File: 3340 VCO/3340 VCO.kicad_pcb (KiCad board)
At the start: 2 copper layers, 99 parts, among them J1 AudioJack2_SwitchT, J2 AudioJack2_SwitchT, J3 AudioJack2_SwitchT, J4 AudioJack2_SwitchT, J5 AudioJack2_SwitchT, J6 Conn_02x05_Odd_Even, J7 AudioJack2_SwitchT, J8 AudioJack2_SwitchT, J9 AudioJack2_SwitchT, SW1 SW_SPDT, U1 TL072, U2 TL072, U3 TL072, U4 AS3340

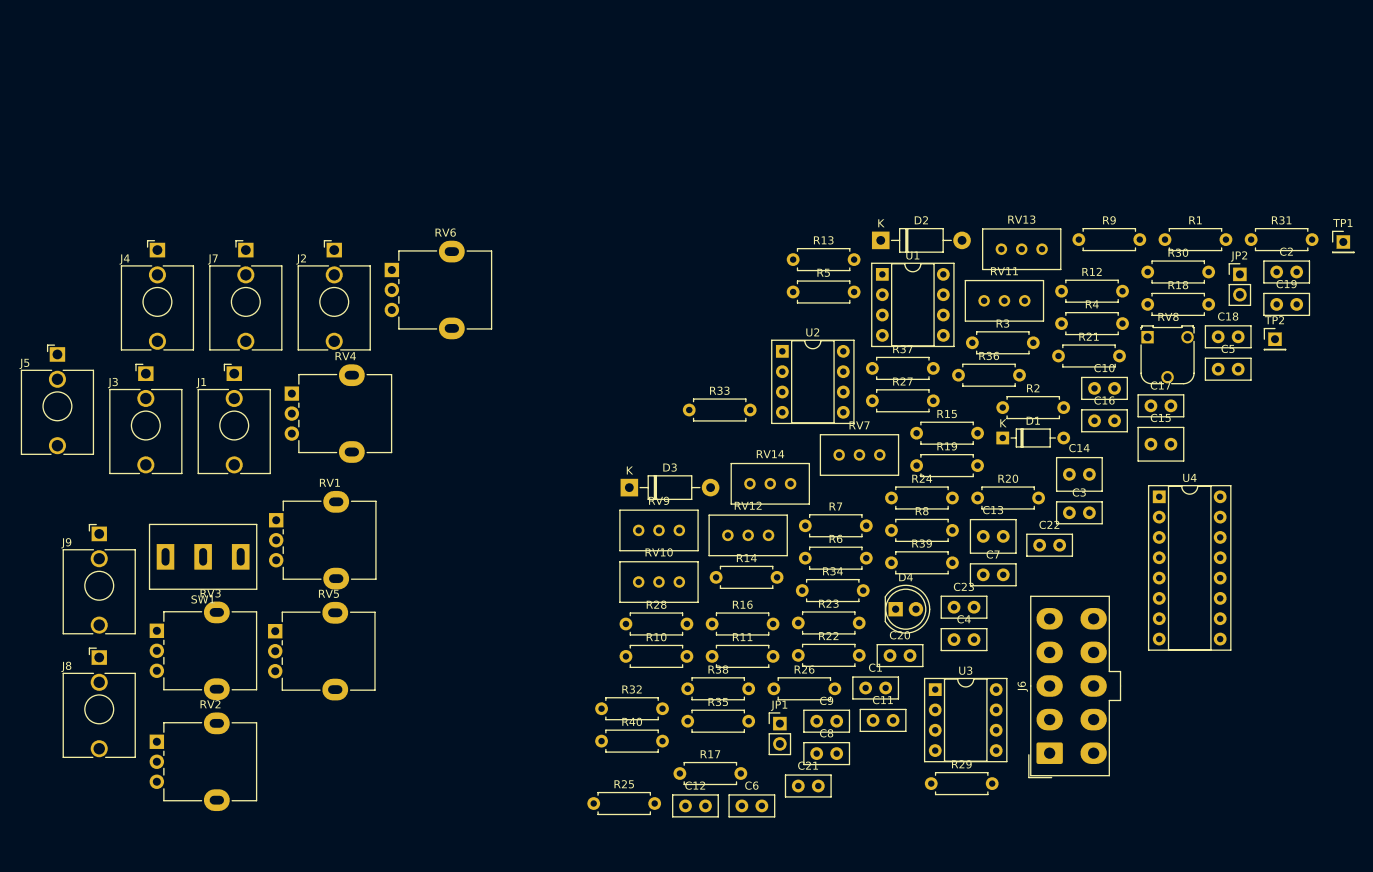
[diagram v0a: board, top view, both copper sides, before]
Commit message: Create separate front end VCO board
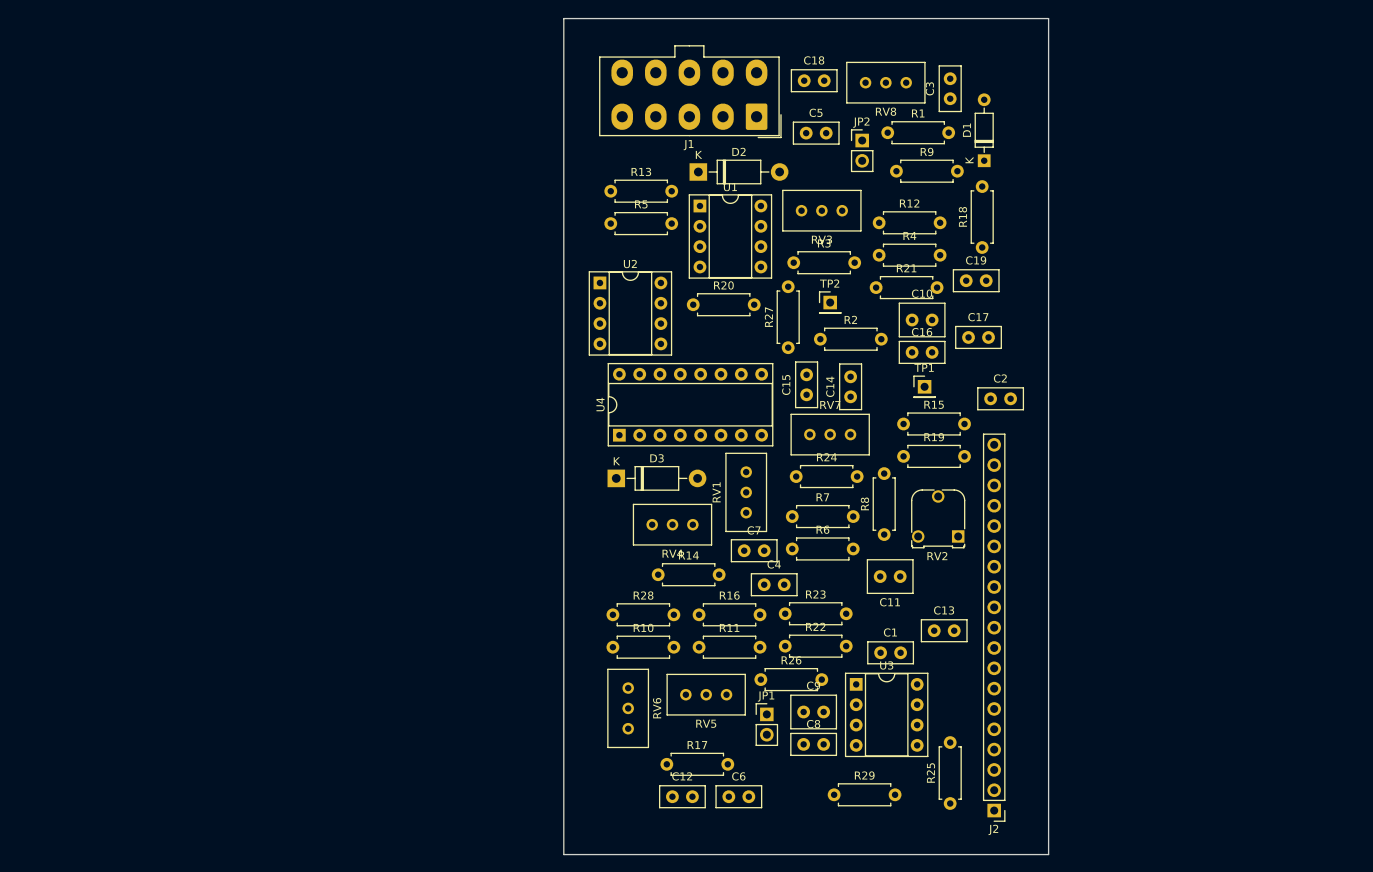
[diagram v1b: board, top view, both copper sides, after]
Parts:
- removed C20, C21, C22: 10p, 0_Capacitor_THT:C_Disc_D5.5mm_W2.5mm_P2.50mm
- removed C23: 47n, 0_Capacitor_THT:C_Disc_D5.5mm_W2.5mm_P2.50mm
- removed D4: LED, LED_THT:LED_D5.0mm
- removed J3, J4, J5, J7, J8, J9: AudioJack2_SwitchT, Connector_Audio:Jack_3.5mm_QingPu_WQP-PJ398SM_Vertical_CircularHoles
- removed J6: Conn_02x05_Odd_Even, Connector_Molex:Molex_Mini-Fit_Jr_5566-10A_2x05_P4.20mm_Vertical
- removed R30, R37: 47k, Resistor_THT:R_Axial_DIN0207_L6.3mm_D2.5mm_P7.62mm_Horizontal
- removed R31: 56k, Resistor_THT:R_Axial_DIN0207_L6.3mm_D2.5mm_P7.62mm_Horizontal
- removed R32: 75k, Resistor_THT:R_Axial_DIN0207_L6.3mm_D2.5mm_P7.62mm_Horizontal
- removed R33, R34, R35: 1k, Resistor_THT:R_Axial_DIN0207_L6.3mm_D2.5mm_P7.62mm_Horizontal
- removed R36: 68k, Resistor_THT:R_Axial_DIN0207_L6.3mm_D2.5mm_P7.62mm_Horizontal
- removed R38: 15k, Resistor_THT:R_Axial_DIN0207_L6.3mm_D2.5mm_P7.62mm_Horizontal
- removed R39, R40: 33k, Resistor_THT:R_Axial_DIN0207_L6.3mm_D2.5mm_P7.62mm_Horizontal
- removed RV10, RV12, RV13, RV14, RV9: 10k, Potentiometer_THT:Potentiometer_Bourns_3296W_Vertical
- removed RV11: 1k, Potentiometer_THT:Potentiometer_Bourns_3296W_Vertical
- removed SW1: SW_SPDT, 0_Switch_THT:MTS-102_MTS-103_MTS-112_MTS-113_MTS-123
- C1: value 0.1u -> 10n
- C10: value 0.1u -> 10u; footprint 0_Capacitor_THT:C_Disc_D5.5mm_W2.5mm_P2.50mm -> 0_Capacitor_THT:C_Disc_D5.5mm_W4.0mm_P2.50mm
- C11: value 0.1u -> 1u; footprint 0_Capacitor_THT:C_Disc_D5.5mm_W2.5mm_P2.50mm -> 0_Capacitor_THT:C_Disc_D5.5mm_W4.0mm_P2.50mm
- C12: value 680p -> 0.1u
- C13, C14: value 10u -> 0.1u; footprint 0_Capacitor_THT:C_Disc_D5.5mm_W4.0mm_P2.50mm -> 0_Capacitor_THT:C_Disc_D5.5mm_W2.5mm_P2.50mm
- C15: value 1u -> 0.1u; footprint 0_Capacitor_THT:C_Disc_D5.5mm_W4.0mm_P2.50mm -> 0_Capacitor_THT:C_Disc_D5.5mm_W2.5mm_P2.50mm
- C16, C17, C18: value 0.1u -> 10p
- C19: value 0.1u -> 47n
- C2: value 1n -> 10p
- C3: value 10p -> 10n
- C4, C5: value 10n -> 0.1u
- C8: value 1n -> 680p
- C9: value 10n -> 10u; footprint 0_Capacitor_THT:C_Disc_D5.5mm_W2.5mm_P2.50mm -> 0_Capacitor_THT:C_Disc_D5.5mm_W4.0mm_P2.50mm
- J1: value AudioJack2_SwitchT -> Conn_02x05_Odd_Even; footprint Connector_Audio:Jack_3.5mm_QingPu_WQP-PJ398SM_Vertical_CircularHoles -> Connector_Molex:Molex_Mini-Fit_Jr_5566-10A_2x05_P4.20mm_Vertical
- J2: value AudioJack2_SwitchT -> Conn_01x19; footprint Connector_Audio:Jack_3.5mm_QingPu_WQP-PJ398SM_Vertical_CircularHoles -> Connector_PinHeader_2.54mm:PinHeader_1x19_P2.54mm_Vertical
- R1: value 100k -> 150k
- R10: value 56k -> 1M
- R11: value 150k -> 15k
- R12: value 470 -> 1.5k
- R13: value 470k -> 510
- R14: value 22k -> 56k
- R15: value 1M -> 56k
- R16, R20: value 1M -> 47k
- R17: value 470 -> 47k
- R18, R19: value 5.6k -> 33k
- R2: value 100k -> 470
- R21: value 15k -> 56k
- R22: value 1.5k -> 75k
- R23: value 510 -> 1k
- R24, R25: value 56k -> 1k
- R26: value 47k -> 68k
- R28: value 33k -> 15k
- R3: value 100k -> 470k
- R4: value 100k -> 56k
- R5: value 100k -> 22k
- R6: value 220k -> 1M
- R7: value 15k -> 470
- R8, R9: value 100k -> 5.6k
- RV1: value 10k -> 100k; footprint 0_Potentiometer_THT:Potentiometer_Alpha_RD901F-40-00D_Single_Vertical_MP -> Potentiometer_THT:Potentiometer_Bourns_3296W_Vertical
- RV2: footprint 0_Potentiometer_THT:Potentiometer_Alpha_RD901F-40-00D_Single_Vertical_MP -> Potentiometer_THT:Potentiometer_Runtron_RM-065_Vertical
- RV3, RV4, RV6: footprint 0_Potentiometer_THT:Potentiometer_Alpha_RD901F-40-00D_Single_Vertical_MP -> Potentiometer_THT:Potentiometer_Bourns_3296W_Vertical
- RV5: value 10k -> 1k; footprint 0_Potentiometer_THT:Potentiometer_Alpha_RD901F-40-00D_Single_Vertical_MP -> Potentiometer_THT:Potentiometer_Bourns_3296W_Vertical
- RV7: value 100k -> 10k
- RV8: footprint Potentiometer_THT:Potentiometer_Runtron_RM-065_Vertical -> Potentiometer_THT:Potentiometer_Bourns_3296W_Vertical
- moved J2 108.2 mm to (168.1, 135.1), turned to 180 degrees
- moved RV2 103.4 mm to (163.6, 100.8), turned to 180 degrees
- moved RV3 96.2 mm to (144.0, 60.1), turned to 180 degrees
- moved J1 72.8 mm to (138.4, 48.3), turned to 180 degrees
- moved U4 67.9 mm to (121.2, 88.2), turned to 90 degrees
- moved RV6 64.5 mm to (122.3, 124.8), turned to -90 degrees
- moved C18 60.8 mm to (144.3, 43.8)
- moved C5 59.4 mm to (144.6, 50.4)
- moved RV1 59.1 mm to (137.1, 92.8), turned to 90 degrees
- moved TP2 55.8 mm to (147.6, 71.6)
- moved TP1 55.4 mm to (159.4, 82.1)
- moved C3 53.9 mm to (162.6, 46.1), turned to 90 degrees
- moved RV5 51.9 mm to (129.5, 120.6), turned to 180 degrees
- moved JP2 50.1 mm to (151.6, 51.3)
- moved RV4 47.9 mm to (125.3, 99.3), turned to 180 degrees
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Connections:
- C1 pad 2: Net-(C1-Pad2) -> GND
- C10 pad 2: +12V -> -12V
- C11 pad 1: -12V -> GND
- C11 pad 2: GND -> Net-(U4-VSSI)
- C12 pad 2: Net-(C12-Pad2) -> Net-(U4-VEE)
- C13 pad 1: +12V -> GND
- C13 pad 2: GND -> +12V
- C14 pad 1: GND -> -12V
- C14 pad 2: -12V -> GND
- C15 pad 2: Net-(C15-Pad2) -> +12V
- C16 pad 1: GND -> Net-(U2A--)
- C17 pad 1: GND -> Net-(U2B--)
- C17 pad 2: +12V -> Net-(C17-Pad2)
- C18 pad 1: -12V -> Net-(U3A--)
- C18 pad 2: GND -> Net-(C18-Pad2)
- C19 pad 1: GND -> Net-(U3B--)
- C19 pad 2: +12V -> /LED
- C2 pad 1: Net-(C2-Pad1) -> /PWM
- C2 pad 2: Net-(C2-Pad2) -> Net-(D1-K)
- C3 pad 2: Net-(C3-Pad2) -> GND
- C4 pad 1: Net-(C4-Pad1) -> GND
- C4 pad 2: GND -> +12V
- C5 pad 1: Net-(C5-Pad1) -> -12V
- C8 pad 2: Net-(C8-Pad2) -> Net-(JP2-B)
- C9 pad 1: GND -> +12V
- C9 pad 2: Net-(C9-Pad2) -> GND
- D1 pad 1: Net-(C3-Pad2) -> Net-(D1-K)
- D1 pad 2: Net-(C3-Pad1) -> /PWM
- JP1 pad 1: Net-(JP1-Pad1) -> /CV
- JP1 pad 2: Net-(JP1-Pad2) -> Net-(JP1-B)
- JP2 pad 2: Net-(C12-Pad2) -> Net-(JP2-B)
- R1 pad 1: +12V -> Net-(R1-Pad1)
- R1 pad 2: Net-(R1-Pad2) -> Net-(JP1-B)
- R10 pad 1: Net-(C3-Pad1) -> Net-(D1-K)
- R10 pad 2: Net-(C3-Pad2) -> Net-(U4-VP)
- R11 pad 1: Net-(R11-Pad1) -> Net-(U4-SCALE1)
- R11 pad 2: Net-(JP1-Pad2) -> Net-(R11-Pad2)
- R12 pad 1: Net-(JP1-Pad2) -> Net-(R12-Pad1)
- R12 pad 2: Net-(C4-Pad1) -> Net-(JP2-B)
- R13 pad 1: Net-(JP1-Pad2) -> Net-(U4-VEE)
- R13 pad 2: Net-(R13-Pad2) -> -12V
- R14 pad 1: Net-(R14-Pad1) -> Net-(U4-VP)
- R14 pad 2: GND -> Net-(U2A--)
- R15 pad 1: Net-(C1-Pad2) -> Net-(R15-Pad1)
- R15 pad 2: Net-(R15-Pad2) -> Net-(U2A--)
- R16 pad 1: Net-(R16-Pad1) -> Net-(U4-VSO)
- R16 pad 2: Net-(R15-Pad2) -> Net-(U2B--)
- R17 pad 1: Net-(R15-Pad2) -> Net-(R17-Pad1)
- R17 pad 2: Net-(C5-Pad1) -> Net-(U2B--)
- R18 pad 1: Net-(C16-Pad2) -> Net-(U1B--)
- R18 pad 2: Net-(R18-Pad2) -> Net-(U3A--)
- R19 pad 1: Net-(C16-Pad2) -> Net-(R19-Pad1)
- R19 pad 2: Net-(R19-Pad2) -> Net-(U3A--)
- R2 pad 1: Net-(R2-Pad1) -> Net-(JP1-B)
- R2 pad 2: -12V -> Net-(C1-Pad1)
- R20 pad 1: Net-(C3-Pad2) -> Net-(U2A--)
- R20 pad 2: Net-(R20-Pad2) -> /PULSE
- R21 pad 1: Net-(R21-Pad1) -> Net-(U2B--)
- R21 pad 2: Net-(R21-Pad2) -> /RAMP
- R22 pad 1: Net-(R22-Pad1) -> Net-(U3A--)
- R22 pad 2: Net-(C12-Pad2) -> /TRI
- R23 pad 2: -12V -> /PULSE
- R24 pad 1: Net-(R20-Pad2) -> Net-(C17-Pad2)
- R24 pad 2: Net-(C20-Pad1) -> /RAMP
- R25 pad 1: Net-(R25-Pad1) -> Net-(C18-Pad2)
- R25 pad 2: Net-(C20-Pad1) -> /TRI
- R26 pad 1: Net-(R26-Pad1) -> /TRI
- R26 pad 2: Net-(C21-Pad1) -> Net-(U3B--)
- R27 pad 1: Net-(R27-Pad1) -> Net-(U3B-+)
- R27 pad 2: Net-(C21-Pad1) -> +12V
- R28 pad 1: Net-(R28-Pad1) -> GND
- R28 pad 2: Net-(C22-Pad1) -> Net-(U3B-+)
- R29 pad 1: Net-(R29-Pad1) -> Net-(U3B--)
- R29 pad 2: Net-(C22-Pad1) -> /LED
- R3 pad 1: Net-(R3-Pad1) -> Net-(JP1-B)
- R3 pad 2: Net-(JP1-Pad2) -> Net-(R3-Pad2)
- R4 pad 1: Net-(J2-PadT) -> /PWM
- R4 pad 2: Net-(JP1-Pad2) -> Net-(D1-K)
- R5 pad 2: Net-(JP1-Pad1) -> GND
- R6 pad 2: Net-(JP1-Pad1) -> /FM_LIN
- R7 pad 1: Net-(R7-Pad1) -> /FM_LIN
- R7 pad 2: Net-(R7-Pad2) -> Net-(C3-Pad1)
- R8 pad 1: Net-(R8-Pad1) -> Net-(U4-VEE)
- R8 pad 2: Net-(C3-Pad1) -> Net-(R8-Pad2)
- R9 pad 1: Net-(R7-Pad2) -> Net-(U4-VEE)
- R9 pad 2: Net-(C3-Pad1) -> Net-(U4-SCALE2)
- RV1 pad 1: GND -> +12V
- RV1 pad 2: Net-(R3-Pad1) -> Net-(R1-Pad1)
- RV1 pad 3: Net-(J1-PadT) -> Net-(R1-Pad1)
- RV2 pad 1: -12V -> Net-(U4-VHFT)
- RV2 pad 2: Net-(R5-Pad1) -> Net-(R3-Pad2)
- RV2 pad 3: +12V -> GND
- RV3 pad 1: Net-(R2-Pad1) -> +12V
- RV3 pad 3: Net-(R1-Pad2) -> Net-(R5-Pad1)
- RV4 pad 1: GND -> Net-(R8-Pad2)
- RV4 pad 2: Net-(C1-Pad1) -> Net-(R8-Pad2)
- RV4 pad 3: Net-(J3-PadT) -> Net-(R11-Pad2)
- RV5 pad 2: Net-(R8-Pad1) -> GND
- RV5 pad 3: Net-(J5-PadT) -> Net-(R12-Pad1)
- RV6 pad 1: -12V -> GND
- RV6 pad 2: Net-(R7-Pad1) -> Net-(R15-Pad1)
- RV6 pad 3: +12V -> -12V
- RV7 pad 1: +12V -> GND
- RV7 pad 2: Net-(R11-Pad1) -> Net-(R17-Pad1)
- RV7 pad 3: Net-(R11-Pad1) -> -12V
- RV8 pad 1: Net-(RV8-Pad1) -> GND
- RV8 pad 2: Net-(R13-Pad2) -> Net-(R19-Pad1)
- RV8 pad 3: GND -> -12V
- TP1 pad 1: Net-(R18-Pad2) -> Net-(R8-Pad2)
- TP2 pad 1: Net-(R19-Pad2) -> Net-(U4-SCALE2)
- U1 pad 1: Net-(C3-Pad2) -> Net-(D1-K)
- U1 pad 2: Net-(C3-Pad1) -> /PWM
- U1 pad 6: Net-(R28-Pad1) -> Net-(U1B--)
- U1 pad 7: Net-(R28-Pad1) -> Net-(U1B--)
- U2 pad 1: Net-(C20-Pad2) -> Net-(C16-Pad2)
- U2 pad 2: Net-(C20-Pad1) -> Net-(U2A--)
- U2 pad 6: Net-(C21-Pad1) -> Net-(U2B--)
- U2 pad 7: Net-(C21-Pad2) -> Net-(C17-Pad2)
- U3 pad 1: Net-(C22-Pad2) -> Net-(C18-Pad2)
- U3 pad 2: Net-(C22-Pad1) -> Net-(U3A--)
- U3 pad 5: Net-(R37-Pad1) -> Net-(U3B-+)
- U3 pad 6: Net-(C23-Pad1) -> Net-(U3B--)
- U3 pad 7: Net-(C23-Pad2) -> /LED
- U4 pad 1: Net-(R21-Pad1) -> Net-(U4-SCALE1)
- U4 pad 11: Net-(SW1-Pad2) -> /CAP
- U4 pad 13: Net-(R15-Pad2) -> /FM_LIN
- U4 pad 14: Net-(C12-Pad2) -> Net-(JP2-B)
- U4 pad 15: Net-(JP1-Pad2) -> Net-(JP1-B)
- U4 pad 2: Net-(R19-Pad2) -> Net-(U4-SCALE2)
- U4 pad 3: Net-(C16-Pad2) -> Net-(U4-VEE)
- U4 pad 4: Net-(R20-Pad2) -> Net-(U4-VP)
- U4 pad 5: Net-(C3-Pad2) -> Net-(D1-K)
- U4 pad 6: Net-(C2-Pad2) -> /HS
- U4 pad 7: Net-(RV8-Pad1) -> Net-(U4-VHFT)
- U4 pad 8: Net-(R26-Pad1) -> Net-(U4-VSO)
- U4 pad 9: Net-(C15-Pad2) -> Net-(U4-VSSI)
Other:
- board outline added: 60.6 x 104.5 mm

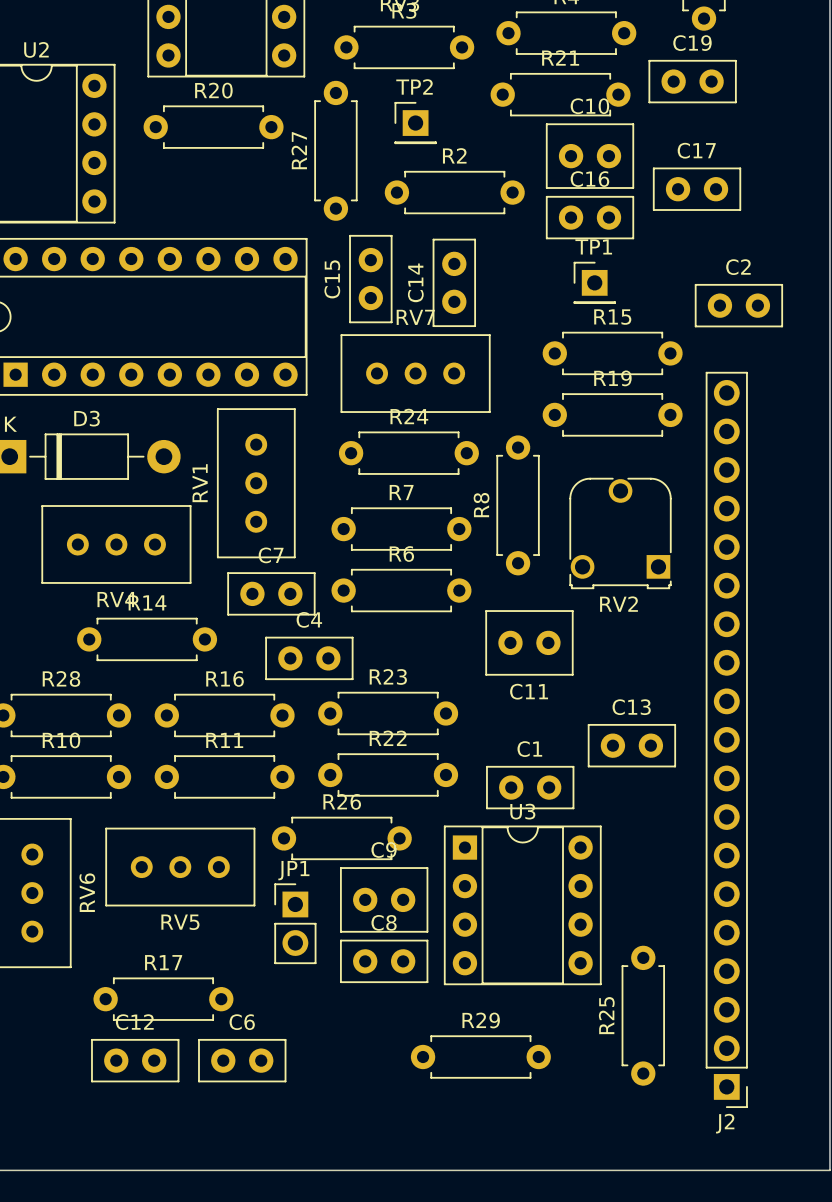
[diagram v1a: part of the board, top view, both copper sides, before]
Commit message: Add -5V regulator
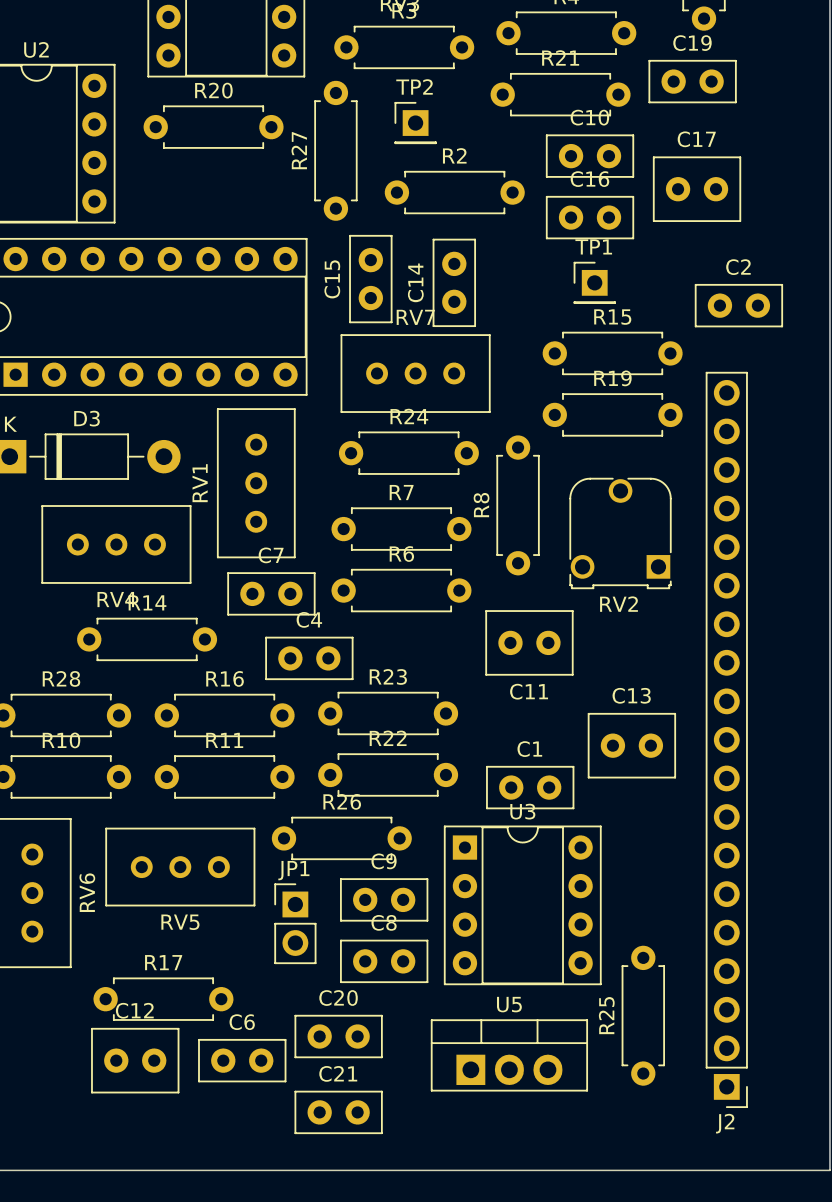
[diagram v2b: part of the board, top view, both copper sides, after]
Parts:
- removed R29: 33k, Resistor_THT:R_Axial_DIN0207_L6.3mm_D2.5mm_P7.62mm_Horizontal
- added C20: 10p, 0_Capacitor_THT:C_Disc_D5.5mm_W2.5mm_P2.50mm, F.Cu at (141.2, 131.8)
- added C21: 47n, 0_Capacitor_THT:C_Disc_D5.5mm_W2.5mm_P2.50mm, F.Cu at (141.2, 136.8)
- added U5: MC7905, Package_TO_SOT_THT:TO-220-3_Vertical, F.Cu at (151.2, 133.9)
- C10: value 10u -> 680p; footprint 0_Capacitor_THT:C_Disc_D5.5mm_W4.0mm_P2.50mm -> 0_Capacitor_THT:C_Disc_D5.5mm_W2.5mm_P2.50mm
- C11: value 1u -> 10u
- C12: value 0.1u -> 10u; footprint 0_Capacitor_THT:C_Disc_D5.5mm_W2.5mm_P2.50mm -> 0_Capacitor_THT:C_Disc_D5.5mm_W4.0mm_P2.50mm
- C13: value 0.1u -> 1u; footprint 0_Capacitor_THT:C_Disc_D5.5mm_W2.5mm_P2.50mm -> 0_Capacitor_THT:C_Disc_D5.5mm_W4.0mm_P2.50mm
- C15: value 0.1u -> 0.33u
- C16: value 10p -> 0.1u
- C17: value 10p -> 1u; footprint 0_Capacitor_THT:C_Disc_D5.5mm_W2.5mm_P2.50mm -> 0_Capacitor_THT:C_Disc_D5.5mm_W4.0mm_P2.50mm
- C19: value 47n -> 10p
- C3: value 10n -> 0.1u
- C5: value 0.1u -> 10n
- C8: value 680p -> 0.1u
- C9: value 10u -> 0.1u; footprint 0_Capacitor_THT:C_Disc_D5.5mm_W4.0mm_P2.50mm -> 0_Capacitor_THT:C_Disc_D5.5mm_W2.5mm_P2.50mm
- R13: value 510 -> 56k
- R15: value 56k -> 47k
- R17: value 47k -> 33k
- R19: value 33k -> 47k
- R20: value 47k -> 56k
- R21: value 56k -> 75k
- R22: value 75k -> 1k
- R25: value 1k -> 68k
- R26: value 68k -> 47k
- R27: value 47k -> 15k
- R28: value 15k -> 33k
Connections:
- C10 pad 2: -12V -> Net-(JP2-B)
- C11 pad 1: GND -> +12V
- C11 pad 2: Net-(U4-VSSI) -> GND
- C12 pad 2: Net-(U4-VEE) -> -12V
- C13 pad 2: +12V -> Net-(U4-VSSI)
- C14 pad 1: -12V -> GND
- C14 pad 2: GND -> -5V
- C15 pad 2: +12V -> -12V
- C16 pad 1: Net-(U2A--) -> GND
- C16 pad 2: Net-(C16-Pad2) -> +12V
- C17 pad 1: Net-(U2B--) -> GND
- C17 pad 2: Net-(C17-Pad2) -> -5V
- C18 pad 1: Net-(U3A--) -> Net-(U2A--)
- C19 pad 1: Net-(U3B--) -> Net-(U2B--)
- C19 pad 2: /LED -> Net-(C19-Pad2)
- C3 pad 1: Net-(C3-Pad1) -> GND
- C3 pad 2: GND -> +12V
- C4 pad 1: GND -> -12V
- C4 pad 2: +12V -> GND
- C5 pad 1: -12V -> Net-(C5-Pad1)
- C8 pad 2: Net-(JP2-B) -> +12V
- C9 pad 1: +12V -> -12V
- R13 pad 1: Net-(U4-VEE) -> Net-(U4-VP)
- R13 pad 2: -12V -> Net-(U2A--)
- R14 pad 1: Net-(U4-VP) -> Net-(R14-Pad1)
- R15 pad 1: Net-(R15-Pad1) -> Net-(U4-VSO)
- R15 pad 2: Net-(U2A--) -> Net-(U2B--)
- R16 pad 1: Net-(U4-VSO) -> Net-(R16-Pad1)
- R17 pad 1: Net-(R17-Pad1) -> Net-(U1B--)
- R17 pad 2: Net-(U2B--) -> Net-(U3A--)
- R18 pad 1: Net-(U1B--) -> Net-(R18-Pad1)
- R19 pad 1: Net-(R19-Pad1) -> Net-(U2A--)
- R19 pad 2: Net-(U3A--) -> /PULSE
- R20 pad 1: Net-(U2A--) -> Net-(U2B--)
- R20 pad 2: /PULSE -> /RAMP
- R21 pad 1: Net-(U2B--) -> Net-(U3A--)
- R21 pad 2: /RAMP -> /TRI
- R22 pad 1: Net-(U3A--) -> Net-(C18-Pad2)
- R22 pad 2: /TRI -> /PULSE
- R23 pad 1: Net-(C16-Pad2) -> Net-(C19-Pad2)
- R23 pad 2: /PULSE -> /RAMP
- R24 pad 1: Net-(C17-Pad2) -> Net-(C20-Pad2)
- R24 pad 2: /RAMP -> /TRI
- R25 pad 1: Net-(C18-Pad2) -> /TRI
- R25 pad 2: /TRI -> Net-(U3B--)
- R26 pad 1: /TRI -> Net-(U3B-+)
- R26 pad 2: Net-(U3B--) -> +12V
- R27 pad 1: Net-(U3B-+) -> GND
- R27 pad 2: +12V -> Net-(U3B-+)
- R28 pad 1: GND -> Net-(U3B--)
- R28 pad 2: Net-(U3B-+) -> /LED
- R7 pad 2: Net-(C3-Pad1) -> Net-(C5-Pad1)
- R8 pad 1: Net-(U4-VEE) -> -5V
- R9 pad 1: Net-(U4-VEE) -> -5V
- RV6 pad 2: Net-(R15-Pad1) -> Net-(R14-Pad1)
- RV7 pad 2: Net-(R17-Pad1) -> Net-(R16-Pad1)
- RV8 pad 2: Net-(R19-Pad1) -> Net-(R18-Pad1)
- U2 pad 1: Net-(C16-Pad2) -> Net-(C18-Pad2)
- U2 pad 7: Net-(C17-Pad2) -> Net-(C19-Pad2)
- U3 pad 1: Net-(C18-Pad2) -> Net-(C20-Pad2)
- U4 pad 3: Net-(U4-VEE) -> -5V

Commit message: Update VCO capacitor selection
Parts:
- removed U5: MC7905, Package_TO_SOT_THT:TO-220-3_Vertical
- added D4: 1N5819, Diode_THT:D_DO-41_SOD81_P10.16mm_Horizontal, F.Cu at (162.2, 139.1)
- added H1: MNT_STANDOFF, 0_MountingHole:MountingHole_Pitch7.5mm_Drill3.4mm, F.Cu at (167.8, 44.5)
- added H2: MNT_STANDOFF, 0_MountingHole:MountingHole_Pitch7.5mm_Drill3.4mm, F.Cu at (119.5, 135.2)
- added U6: LM7905_TO220, Package_TO_SOT_THT:TO-220-3_Vertical, F.Cu at (150.9, 135.2)
- C15: value 0.33u -> 2.2u; footprint 0_Capacitor_THT:C_Disc_D5.5mm_W2.5mm_P2.50mm -> Capacitor_THT:CP_Radial_Tantal_D5.5mm_P2.50mm
- C17: footprint 0_Capacitor_THT:C_Disc_D5.5mm_W4.0mm_P2.50mm -> Capacitor_THT:CP_Radial_Tantal_D5.0mm_P2.50mm
- moved C3 23.1 mm to (171.8, 67.2)
- moved R25 8.14 mm to (163.0, 126.1)
- moved D1 7.74 mm to (171.8, 59.8)
- moved R8 1.01 mm to (154.5, 101.6)

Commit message: Finish VCO
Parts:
- C1, C10, C11, C12, C13, C14, C15, C16, C17, C18, C19, C2, C20, C21, C3, C4, C5, C6, C7, C8, C9, D1, D2, D3, D4, JP1, JP2, R1, R10, R11, R12, R13, R14, R15, R16, R17, R18, R19, R2, R20, R21, R22, R23, R24, R25, R26, R27, R28, R3, R4, R5, R6, R7, R8, R9, RV1, RV2, RV3, RV4, RV5, RV6, RV7, RV8, TP1, TP2, U1, U2, U3, U4, U6: moved to B.Cu
- J1: value Conn_02x05_Odd_Even -> Conn_02x05_Top_Bottom; moved to B.Cu
- moved H1 102.1 mm to (120.1, 134.8)
- moved C6 95.4 mm to (145.2, 38.5), turned to 180 degrees
- moved RV8 90.8 mm to (156.6, 134.8), turned to 0 degrees
- moved J2 83.8 mm to (137.2, 57.2), turned to 0 degrees
- moved H2 82.9 mm to (153.5, 59.6)
- moved RV6 80.9 mm to (166.3, 57.0), turned to 0 degrees
- moved R22 74.4 mm to (156.2, 41.5)
- moved R23 66.9 mm to (136.8, 43.8), turned to 180 degrees
- moved R18 65.7 mm to (157.3, 129.8), turned to 180 degrees
- moved R14 64.7 mm to (161.1, 51.2), turned to 180 degrees
- moved U1 64.4 mm to (162.8, 115.7), turned to 180 degrees
- moved R21 60.7 mm to (143.8, 129.6), turned to -90 degrees
- moved R4 58.1 mm to (171.9, 120.8), turned to 90 degrees
- moved D1 53.4 mm to (168.9, 113.2), turned to -90 degrees
- moved R9 53.1 mm to (144.4, 107.0)
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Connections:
- J1 pad 2: +12V -> GND
- J1 pad 3: GND -> Chassis
- J1 pad 5: Chassis -> -12V
- J1 pad 6: Chassis -> +12V
- J1 pad 8: GND -> Chassis
- J1 pad 9: -12V -> GND
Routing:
- net +12V: track 0.00 -> 244.8 mm, vias 0 -> 5
- net -12V: track 0.00 -> 212.7 mm, vias 0 -> 7
- net Net-(U4-VSO): track 0.00 -> 113.5 mm, vias 0 -> 5
- net /TRI: track 0.00 -> 109.6 mm, vias 0 -> 3
- net Net-(U4-VP): track 0.00 -> 89.5 mm, vias 0 -> 3
- net /PWM: track 0.00 -> 75.8 mm, vias 0 -> 4
- net /PULSE: track 0.00 -> 69.5 mm
- net -5V: track 0.00 -> 63.4 mm, vias 0 -> 1
- net /LED: track 0.00 -> 59.8 mm, vias 0 -> 3
- net Net-(U1B-+): track 0.00 -> 52.4 mm, vias 0 -> 1
- net Chassis: track 0.00 -> 48.9 mm
- net /FM_LIN: track 0.00 -> 45.9 mm
- net Net-(D1-K): track 0.00 -> 44.2 mm, vias 0 -> 1
- net /RAMP: track 0.00 -> 40.0 mm
- net /HS: track 0.00 -> 36.5 mm, vias 0 -> 2
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- added copper zone on B.Cu, net GND
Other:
- board text added: "JLCJLCJLCJLC"
- board text added: "VCO V1 Matthew Taylor"
